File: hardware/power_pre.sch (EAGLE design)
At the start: 65 parts, among them IC1 7815, IC2 7915, IC3 7805, IC4 7905, IC5 7805

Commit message: tweaks
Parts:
- added C30, C33: 10uF, rcl:CPOL-EU153CLV-0405
- added C31, C32, C34: 100n, rcl:C-EUC0805
- added JP1: spdif, SparkFun-Connectors:M02PTH
- added U$1: DEGSON_8, Simplex-Connectors:DEGSON_8
- added U1: V_REG_LDOSMD, SparkFun-PowerIC:V_REG_LDOSMD
- added X1: 2512-5, Simplex-Connectors:2512-5
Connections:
- new net +3V3D: C30.+, C32.2, U1.OUT, X1-11.KL
- new net N$7: C34.2, U1.BP
- net +15VA: now also X1-1.KL
- net +5VA: now also X1-5.KL
- net +5VD: now also C31.2, C33.+, U1.EN, U1.IN, X1-9.KL
- net -15VA: now also X1-3.KL
- net -5VA: now also X1-7.KL
- net 15VAC_1: now also U$1G$3.KL
- net 15VAC_2: now also U$1G$4.KL
- net 15VAC_3: now also U$1G$1.KL
- net 15VAC_4: now also U$1G$2.KL
- net 5VAC_1: now also U$1G$5.KL
- net 5VAC_2: now also U$1G$6.KL
- net 5VAC_3: now also U$1G$7.KL
- net 5VAC_4: now also U$1G$8.KL
- net GND: now also C30.-, C31.1, C32.1, C33.-, C34.1, JP1.1, U1.GND, X1-10.KL, X1-12.KL, X1-2.KL, X1-4.KL, X1-6.KL, X1-8.KL
- net SPDIF: now also JP1.2

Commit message: tweak filters
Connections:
- net -15VA: now also D7.A; no longer D7.C
- net -5VA: now also D8.A; no longer D8.C
- net GND: now also D7.C, D8.C; no longer D7.A, D8.A
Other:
- moved on the sheet: D7, D8
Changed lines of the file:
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@@
 <instance part="B2" gate="G$1" x="132.08" y="88.9" rot="R90"/>
 <instance part="D6" gate="G$1" x="203.2" y="175.26" rot="R90"/>
-<instance part="D7" gate="G$1" x="203.2" y="104.14" rot="R270"/>
+<instance part="D7" gate="G$1" x="203.2" y="104.14" rot="R90"/>
 <instance part="C5" gate="G$1" x="160.02" y="177.8"/>
 <instance part="IC1" gate="IC$1" x="175.26" y="185.42"/>
@@
 <instance part="B4" gate="G$1" x="269.24" y="88.9" rot="R90"/>
 <instance part="D5" gate="G$1" x="342.9" y="175.26" rot="R90"/>
-<instance part="D8" gate="G$1" x="342.9" y="104.14" rot="R270"/>
+<instance part="D8" gate="G$1" x="342.9" y="104.14" rot="R90"/>
 <instance part="IC3" gate="IC$1" x="314.96" y="185.42"/>
 <instance part="IC4" gate="G$1" x="314.96" y="88.9"/>
@@
 <segment>
 <pinref part="IC2" gate="G$1" pin="VO"/>
-<pinref part="D7" gate="G$1" pin="C"/>
 <wire x1="185.42" y1="88.9" x2="193.04" y2="88.9" width="0.1524" layer="91"/>
 <wire x1="193.04" y1="88.9" x2="203.2" y2="88.9" width="0.1524" layer="91"/>
-<wire x1="203.2" y1="88.9" x2="203.2" y2="101.6" width="0.1524" layer="91"/>
 <pinref part="D1" gate="G$1" pin="C"/>
+<wire x1="203.2" y1="88.9" x2="208.28" y2="88.9" width="0.1524" layer="91"/>
 <wire x1="177.8" y1="76.2" x2="193.04" y2="76.2" width="0.1524" layer="91"/>
 <wire x1="193.04" y1="76.2" x2="193.04" y2="88.9" width="0.1524" layer="91"/>
 <junction x="193.04" y="88.9"/>
-<wire x1="203.2" y1="88.9" x2="208.28" y2="88.9" width="0.1524" layer="91"/>
-<junction x="203.2" y="88.9"/>
 <label x="208.28" y="88.9" size="1.778" layer="95"/>
 <pinref part="C22" gate="G$1" pin="-"/>
 <wire x1="193.04" y1="99.06" x2="193.04" y2="88.9" width="0.1524" layer="91"/>
+<pinref part="D7" gate="G$1" pin="A"/>
+<wire x1="203.2" y1="101.6" x2="203.2" y2="88.9" width="0.1524" layer="91"/>
+<junction x="203.2" y="88.9"/>
 </segment>
 <segment>
@@
 <pinref part="C24" gate="G$1" pin="-"/>
 <wire x1="332.74" y1="101.6" x2="332.74" y2="91.44" width="0.1524" layer="91"/>
-<pinref part="D8" gate="G$1" pin="C"/>
-<wire x1="342.9" y1="91.44" x2="342.9" y2="101.6" width="0.1524" layer="91"/>
-<wire x1="342.9" y1="91.44" x2="345.44" y2="91.44" width="0.1524" layer="91"/>
 <label x="345.44" y="91.44" size="1.778" layer="95"/>
 <wire x1="332.74" y1="91.44" x2="342.9" y2="91.44" width="0.1524" layer="91"/>
+<pinref part="D8" gate="G$1" pin="A"/>
+<wire x1="342.9" y1="91.44" x2="345.44" y2="91.44" width="0.1524" layer="91"/>
+<wire x1="342.9" y1="101.6" x2="342.9" y2="91.44" width="0.1524" layer="91"/>
 <junction x="342.9" y="91.44"/>
 </segment>
@@
 <segment>
 <wire x1="299.72" y1="109.22" x2="299.72" y2="116.84" width="0.1524" layer="91"/>
-<pinref part="D8" gate="G$1" pin="A"/>
 <wire x1="299.72" y1="116.84" x2="314.96" y2="116.84" width="0.1524" layer="91"/>
 <wire x1="314.96" y1="116.84" x2="332.74" y2="116.84" width="0.1524" layer="91"/>
 <wire x1="332.74" y1="116.84" x2="342.9" y2="116.84" width="0.1524" layer="91"/>
-<wire x1="342.9" y1="116.84" x2="342.9" y2="106.68" width="0.1524" layer="91"/>
 <pinref part="IC4" gate="G$1" pin="GND"/>
 <wire x1="314.96" y1="96.52" x2="314.96" y2="116.84" width="0.1524" layer="91"/>
@@
 <wire x1="350.52" y1="142.24" x2="350.52" y2="139.7" width="0.1524" layer="91"/>
 <junction x="342.9" y="162.56"/>
-<junction x="342.9" y="116.84"/>
 <junction x="342.9" y="142.24"/>
 <pinref part="GND3" gate="1" pin="GND"/>
@@
 <wire x1="269.24" y1="93.98" x2="269.24" y2="116.84" width="0.1524" layer="91"/>
 <junction x="269.24" y="116.84"/>
+<pinref part="D8" gate="G$1" pin="C"/>
+<wire x1="342.9" y1="106.68" x2="342.9" y2="116.84" width="0.1524" layer="91"/>
+<junction x="342.9" y="116.84"/>
 </segment>
 <segment>
 <wire x1="160.02" y1="106.68" x2="160.02" y2="116.84" width="0.1524" layer="91"/>
-<pinref part="D7" gate="G$1" pin="A"/>
 <wire x1="160.02" y1="116.84" x2="175.26" y2="116.84" width="0.1524" layer="91"/>
 <wire x1="175.26" y1="116.84" x2="193.04" y2="116.84" width="0.1524" layer="91"/>
 <wire x1="193.04" y1="116.84" x2="203.2" y2="116.84" width="0.1524" layer="91"/>
-<wire x1="203.2" y1="116.84" x2="203.2" y2="106.68" width="0.1524" layer="91"/>
 <pinref part="IC2" gate="G$1" pin="GND"/>
 <wire x1="175.26" y1="93.98" x2="175.26" y2="116.84" width="0.1524" layer="91"/>
@@
 <wire x1="210.82" y1="142.24" x2="210.82" y2="139.7" width="0.1524" layer="91"/>
 <junction x="203.2" y="162.56"/>
-<junction x="203.2" y="116.84"/>
 <junction x="203.2" y="142.24"/>
 <pinref part="C1" gate="G$1" pin="+"/>
@@
 <wire x1="132.08" y1="93.98" x2="132.08" y2="116.84" width="0.1524" layer="91"/>
 <junction x="132.08" y="116.84"/>
-</segment>
-<segment>
+<pinref part="D7" gate="G$1" pin="C"/>
+<wire x1="203.2" y1="106.68" x2="203.2" y2="116.84" width="0.1524" layer="91"/>
+<junction x="203.2" y="116.84"/>
+</segment>
+<segment>

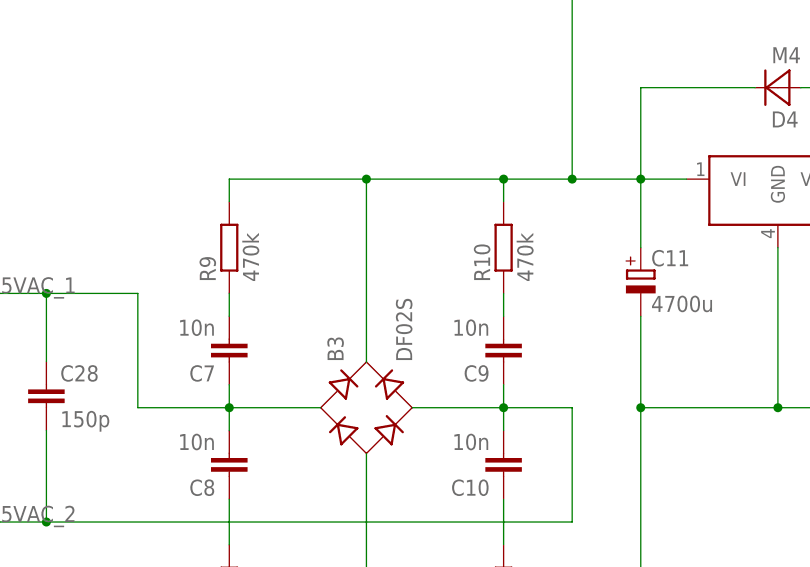
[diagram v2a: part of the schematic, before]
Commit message: change +5v bridge rectifier in power_pre
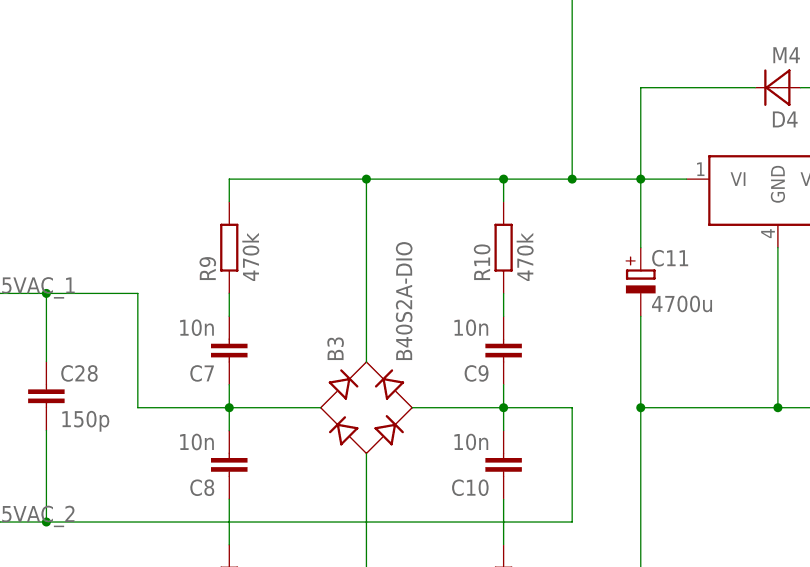
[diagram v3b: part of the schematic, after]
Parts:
- B3: value DF02S -> B40S2A-DIO
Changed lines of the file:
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@@
 <part name="C9" library="rcl" deviceset="C-EU" device="C0805" value="10n"/>
 <part name="C10" library="rcl" deviceset="C-EU" device="C0805" value="10n"/>
-<part name="B3" library="rectifier" deviceset="DF*S" device="" technology="02"/>
+<part name="B3" library="rectifier" deviceset="DF*S" device="" technology="02" value="B40S2A-DIO"/>
 <part name="B4" library="rectifier" deviceset="DF*S" device="" technology="02"/>
 <part name="D5" library="diode" deviceset="MBRA340T3" device="" value="M4"/>

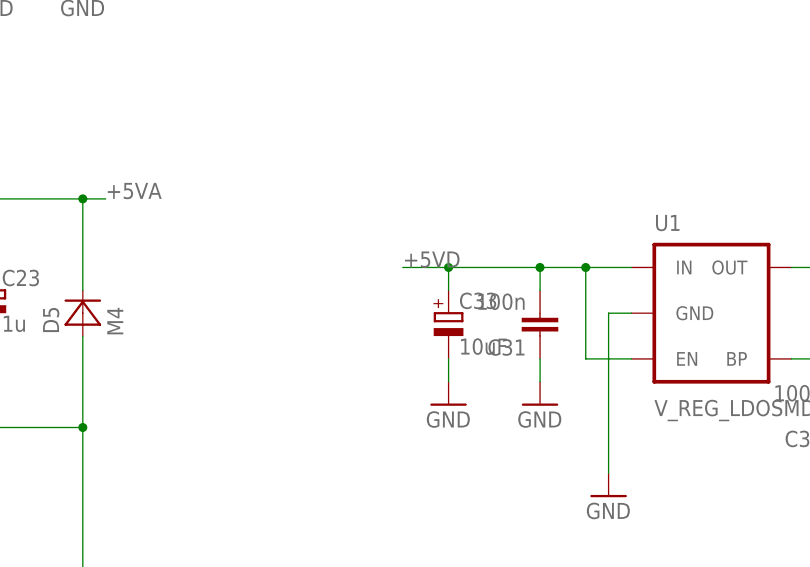
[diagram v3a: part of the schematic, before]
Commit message: add debug window into ncurses cli
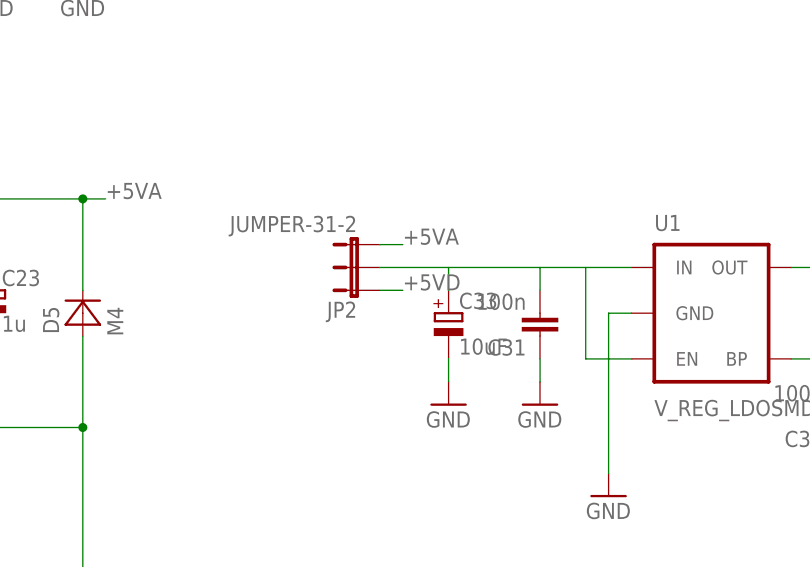
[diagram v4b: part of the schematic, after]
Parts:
- added JP2: JUMPER-31-2, SparkFun-Passives:JUMPER-31-2
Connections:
- new net N$4: C31.2, C33.+, JP2.2, U1.EN, U1.IN
- net +5VA: now also JP2.3
- net +5VD: now also JP2.1; no longer C31.2, C33.+, U1.EN, U1.IN
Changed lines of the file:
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@@
 <part name="JP1" library="SparkFun-Connectors" deviceset="M02" device="PTH" value="spdif"/>
 <part name="GND13" library="supply1" deviceset="GND" device=""/>
+<part name="JP2" library="SparkFun-Passives" deviceset="JUMPER-3" device="1-2"/>
 </parts>
 <sheets>
@@
 <instance part="JP1" gate="G$1" x="274.32" y="236.22"/>
 <instance part="GND13" gate="1" x="284.48" y="223.52"/>
+<instance part="JP2" gate="G$1" x="373.38" y="177.8" rot="R90"/>
 </instances>
 <busses>
@@
 </segment>
 <segment>
-<pinref part="U1" gate="G$1" pin="IN"/>
-<wire x1="378.46" y1="180.34" x2="383.54" y2="180.34" width="0.1524" layer="91"/>
-<pinref part="C31" gate="G$1" pin="2"/>
-<wire x1="383.54" y1="180.34" x2="393.7" y2="180.34" width="0.1524" layer="91"/>
-<wire x1="398.78" y1="180.34" x2="403.86" y2="180.34" width="0.1524" layer="91"/>
-<wire x1="393.7" y1="177.8" x2="393.7" y2="180.34" width="0.1524" layer="91"/>
-<pinref part="C33" gate="G$1" pin="+"/>
-<wire x1="383.54" y1="177.8" x2="383.54" y2="180.34" width="0.1524" layer="91"/>
-<wire x1="393.7" y1="180.34" x2="398.78" y2="180.34" width="0.1524" layer="91"/>
-<wire x1="398.78" y1="180.34" x2="398.78" y2="170.18" width="0.1524" layer="91"/>
-<pinref part="U1" gate="G$1" pin="EN"/>
-<wire x1="398.78" y1="170.18" x2="403.86" y2="170.18" width="0.1524" layer="91"/>
-<junction x="383.54" y="180.34"/>
-<junction x="393.7" y="180.34"/>
-<junction x="398.78" y="180.34"/>
-<label x="378.46" y="180.34" size="1.778" layer="95"/>
+<pinref part="JP2" gate="G$1" pin="1"/>
+<wire x1="375.92" y1="177.8" x2="378.46" y2="177.8" width="0.1524" layer="91"/>
+<label x="378.46" y="177.8" size="1.778" layer="95"/>
 </segment>
 </net>
@@
 <label x="403.86" y="111.76" size="1.778" layer="95"/>
 </segment>
+<segment>
+<pinref part="JP2" gate="G$1" pin="3"/>
+<wire x1="375.92" y1="182.88" x2="378.46" y2="182.88" width="0.1524" layer="91"/>
+<label x="378.46" y="182.88" size="1.778" layer="95"/>
+</segment>
 </net>
 <net name="N$2" class="0">
@@
 </segment>
 </net>
+<net name="N$4" class="0">
+<segment>
+<pinref part="U1" gate="G$1" pin="EN"/>
+<wire x1="403.86" y1="170.18" x2="398.78" y2="170.18" width="0.1524" layer="91"/>
+<pinref part="JP2" gate="G$1" pin="2"/>
+<pinref part="U1" gate="G$1" pin="IN"/>
+<wire x1="375.92" y1="180.34" x2="383.54" y2="180.34" width="0.1524" layer="91"/>
+<wire x1="383.54" y1="180.34" x2="393.7" y2="180.34" width="0.1524" layer="91"/>
+<wire x1="393.7" y1="180.34" x2="398.78" y2="180.34" width="0.1524" layer="91"/>
+<wire x1="398.78" y1="180.34" x2="403.86" y2="180.34" width="0.1524" layer="91"/>
+<wire x1="398.78" y1="170.18" x2="398.78" y2="180.34" width="0.1524" layer="91"/>
+<pinref part="C31" gate="G$1" pin="2"/>
+<wire x1="393.7" y1="177.8" x2="393.7" y2="180.34" width="0.1524" layer="91"/>
+<pinref part="C33" gate="G$1" pin="+"/>
+<wire x1="383.54" y1="177.8" x2="383.54" y2="180.34" width="0.1524" layer="91"/>
+</segment>
+</net>
